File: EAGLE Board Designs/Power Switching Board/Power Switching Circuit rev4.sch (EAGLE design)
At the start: 20 parts, among them Q1 TRANSISTOR_N_MOS_2-7K1S_TK100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, Q2 TRANSISTOR_N_MOS_2-7K1S_TK100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, U1 LOGICGATE_AND_SN74AHCT1G08DBVR, U2 LOGICGATE_INVERTER_SN74AHC1GU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, U3 OPAMP_1_CHANNEL_OPA991, U4 OPAMP_1_CHANNEL_OPA991

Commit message: Created new rev4, removed DCDC, SHDN LED
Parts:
- removed D1: TVS_15V, HyTechDevices:TVS_15V
- removed U$1, U$2: LTC4359IMS8#TRPBF, HyTechDevicesTemp:LTC4359IMS8#TRPBF
- removed U2: LOGICGATE_INVERTER_SN74AHC1GU04DCK3, HyTechDevices:LOGICGATE_INVERTER_SN74AHC1GU04DCK3
- removed U3, U4: OPAMP_1_CHANNEL_OPA991, HyTechDevices:OPAMP_1_CHANNEL_OPA991
- added C10: CAPACITOR_0603_25V_0.1UF, HyTechDevices:CAPACITOR_0603_25V_0.1UF
- added C11: CAPACITOR_0603_10V_1UF, HyTechDevices:CAPACITOR_0603_10V_1UF
- added C12: CAPACITOR_0603_35V_1UF, HyTechDevices:CAPACITOR_0603_35V_1UF
- added C13, C8: CAPACITOR_0603_10V_68NF, HyTechDevices:CAPACITOR_0603_10V_68NF
- added C5, C6: CAPACITOR_0603_25V_47NF, HyTechDevices:CAPACITOR_0603_25V_47NF
- added C7: CAPACITOR_0603_25V_10UF, HyTechDevices:CAPACITOR_0603_25V_10UF
- added C9: CAPACITOR_0603_10V_680PF, HyTechDevices:CAPACITOR_0603_10V_680PF
- added D11, D12: LED_0603_GREEN, HyTechDevices:LED_0603_GREEN
- added D13, D14: LED_0603_YELLOW, HyTechDevices:LED_0603_YELLOW
- added D15, D16: LED_0603_RED, HyTechDevices:LED_0603_RED
- added D17, D7, D8, D9: LED_0603_BLUE, HyTechDevices:LED_0603_BLUE
- added D3: SCHOTTKY_SOD323_30V, HyTechDevices:SCHOTTKY_SOD323_30V
- added D4, D5, D6: TVS_15V, HyTechDevices:TVS_15V
- added J1, J3: CONNECTOR-4_SOURIAU_, HyTechDevices:CONNECTOR-4_SOURIAU_
- added J2: CONNECTOR-3_8STA20435PN, HyTechDevices:CONNECTOR-3_8STA20435PN
- added K1: RELAY_SOLIDSTATE_NO_CMX60D20, HyTechDevicesTemp:RELAY_SOLIDSTATE_NO_CMX60D20
- added Q3, Q4: TRANSISTOR_N_MOS_2-7K1S_TK100S04N1LLQ, HyTechDevices:TRANSISTOR_N_MOS_2-7K1S_TK100S04N1LLQ
- added R10, R25: RESISTOR_0603_5.49K, HyTechDevices:RESISTOR_0603_5.49K
- added R11, R26: RESISTOR_0603_1.13M, HyTechDevices:RESISTOR_0603_1.13M
- added R12, R13, R14, R16, R17, R18, R19, R20, R21: RESISTOR_0603_1K, HyTechDevices:RESISTOR_0603_1K
- added R22: RESISTOR_0603_10K, HyTechDevices:RESISTOR_0603_10K
- added R23, R7: RESISTOR_0603_41.2K, HyTechDevices:RESISTOR_0603_41.2K
- added R24, R9: RESISTOR_0603_13K, HyTechDevices:RESISTOR_0603_13K
- added R8: RESISTOR_0805_0.62, HyTechDevices:RESISTOR_0805_0.62
- added TP1, TP10, TP11, TP12, TP2, TP3, TP4, TP5, TP6, TP7, TP8, TP9: TEST_POINT, HyTechDevices:TEST_POINT
- added XF1, XF2, XF3, XF4: FUSE_HOLDER_MINIBLADEPTH, HyTechDevices:FUSE_HOLDER_MINIBLADEPTH
- C1: value CAPACITOR_0603_25V_1UF -> EEUFP1E681; device HyTechDevices:CAPACITOR_0603_25V_1UF -> HyTechDevicesTemp:EEUFP1E681
- C2, C4: value CAPACITOR_0603_25V_1UF -> CAPACITOR_0603_25V_10UF; device HyTechDevices:CAPACITOR_0603_25V_1UF -> HyTechDevices:CAPACITOR_0603_25V_10UF
- D2: value TVS_15V -> SCHOTTKY_SOD323_30V; device HyTechDevices:TVS_15V -> HyTechDevices:SCHOTTKY_SOD323_30V
- R1, R2: value RESISTOR_0603_1K -> RESISTOR_0603_10K; device HyTechDevices:RESISTOR_0603_1K -> HyTechDevices:RESISTOR_0603_10K
- R4, R5: value RESISTOR_0603_10K -> RESISTOR_SENSE__WSL40262L000FEB; device HyTechDevices:RESISTOR_0603_10K -> HyTechDevicesTemp:RESISTOR_SENSE__WSL40262L000FEB
- R6: value RESISTOR_0603_10K -> RESISTOR_0805_0.62; device HyTechDevices:RESISTOR_0603_10K -> HyTechDevices:RESISTOR_0805_0.62
- U1: value LOGICGATE_AND_SN74AHCT1G08DBVR -> LTC4421; device HyTechDevices:LOGICGATE_AND_SN74AHCT1G08DBVR -> HyTechDevices:LTC4421
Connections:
- removed net +5V: U1P.VDD, U2P.VDD, U3A.VIN-, U3P.VDD, U4A.VIN-, U4P.VDD
- removed net N$10: U$2.!SHDN
- removed net N$14: R3.1, R4.2, U3A.VIN+
- removed net N$16: R3.2
- new net !CH1: D13.C, U1.!CH1
- new net !CH2: D14.C, U1.!CH2
- new net !FAULT1: D15.C, U1.!FAULT1
- new net !FAULT2: D16.C, U1.!FAULT2
- new net !SHDN: D2.C, D3.C, K1.CONTROL+, R3.2, TP11.1, U1.!DISABLE1, U1.!DISABLE2, U1.!SHDN
- new net !VALID1: D11.C, U1.!VALID1
- new net !VALID2: D12.C, U1.!VALID2
- new net BATTERY: J1.1, J1.2, TP1.1, XF1.2, XF2.1
- new net BATTIN: D5.C, K1.CONTACT2, Q3.D, R11.2, R13.2, R6.2, U1.V2
- new net CONVOUT: TP8.1
- new net CPO: C12.2, TP12.1, U1.CPO
- new net DCDC_VICOR: J3.1, J3.2, TP4.1, XF4.1
- new net DCDC_VICORPREMOS: D6.C, Q4.D, R12.2, R26.2, R8.2, U1.V1, XF4.2
- new net GATE1: C6.2, Q1.G, Q4.G, TP9.1, U1.GATE1
- new net GATE2: C5.2, Q2.G, Q3.G, TP2.1, U1.GATE2
- new net GLVMS: D2.A, J2.2, R2.2
- new net INTVDD: C11.1, R14.2, TP3.1, U1.CASIN, U1.INTVDD
- new net N$17: D13.A, R18.1
- new net N$18: R5.3, U1.SENSE2
- new net N$19: D12.A, R17.1
- new net N$20: R5.4, U1.OUT2
- new net N$21: D11.A, R16.1
- new net N$22: C7.1, R8.1
- new net N$23: R4.3, U1.SENSE1
- new net N$24: R24.2, R25.1, U1.UVR1
- new net N$25: R23.2, R24.1, U1.OV1
- new net N$26: R10.2, R11.1, U1.UVF2
- new net N$27: R10.1, R9.2, U1.UVR2
- new net N$28: R7.2, R9.1, U1.OV2
- new net N$30: Q2.D, R5.1
- new net N$31: R4.4, U1.OUT1
- new net N$33: Q1.D, R4.1
- new net OUT: J1.3, J1.4, TP7.1, XF2.2, XF3.2
- new net OUTPREFUSE: C1.PLUS, C10.2, C12.1, C2.1, C3.1, D4.C, R22.2, R4.2, R5.2, U1.CPOREF, U1.EXTVDD, XF3.1
- new net SOURCE1: C6.1, Q1.S, Q4.S, TP10.1, U1.SOURCE1
- new net SOURCE2: C5.1, Q2.S, Q3.S, TP5.1, U1.SOURCE2
- new net START: D3.A, J2.3, R1.2
- new net UVF1: R25.2, R26.1, U1.UVF1
- net GND: now also C1.MINUS, C10.1, C11.2, C13.2, C2.2, C3.2, C4.2, C7.2, C8.2, C9.2, D17.C, D4.A, D5.A, D6.A, D7.C, D8.C, D9.C, J2.1, K1.CONTROL-, R23.1, R3.1, R7.1, TP6.1, U1.GND, U1.RETRY; no longer R4.1, R6.1, U1P.GND, U2P.GND, U3P.GND, U4P.GND
- net N$1: now also C9.1, U1.QUAL; no longer Q1.G, U$1.GATE
- net N$11: now also D16.A, R21.1; no longer U2A.IN, U4A.VOUT
- net N$12: now also K1.CONTACT1, XF1.1; no longer U1A.IN1, U3A.VOUT
- net N$13: now also D15.A, R20.1; no longer R5.1, R6.2, U4A.VIN+
- net N$15: now also D14.A, R19.1; no longer R5.2
- net N$2: now also C13.1, U1.TMR1; no longer Q2.G, U$2.GATE
- net N$3: now also C8.1, U1.TMR2; no longer C1.1, C2.1, C3.1, C4.1, Q1.D, Q2.D, U$1.OUT, U$2.OUT
- net N$4: now also C4.1, R6.1; no longer U1A.IN2, U2A.!IN
- net N$5: now also D17.A, R22.1; no longer D1.C, Q1.S, U$1.IN, U$1.SOURCE
- net N$6: now also D8.A, R13.1; no longer D2.C, Q2.S, U$2.IN, U$2.SOURCE
- net N$7: now also D7.A, R12.1; no longer C3.2, C4.2, D1.A, R1.2, U$1.VSS
- net N$8: now also R16.2, R17.2, R18.2, R19.2, R20.2, R21.2; no longer C1.2, C2.2, D2.A, R2.2, U$2.VSS
- net N$9: now also D9.A, R14.1; no longer U$1.!SHDN, U1A.OUT
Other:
- note added: "10A Fuse"
- note added: "DCDC_VICOR: OV Rising: 14.44V OV Falling: 12.34V UV Rising: 10.98V UV Falling: 9.97V CONVOUT: OV Rising: 14.44V OV Falling: 12.34V UV Rising: 10.98V UV Falling: 9.97V"
- note added: "ILim = 12.5A"
- note added: "VALID1: DCDC_VICOR is within OV/UV for time tValid VALID2: CONVOUT is within OV/UV for time tValid CH1: DCDC_VICOR is the output CH2: CONVOUT is the output FAULT1: Current limit fault on DCDC_VICOR FAULT2: Current limit fault on CONVOUT"
- note added: "tTMR,FLT = 5.644ms"
- note added: "tValid = 10.88ms"

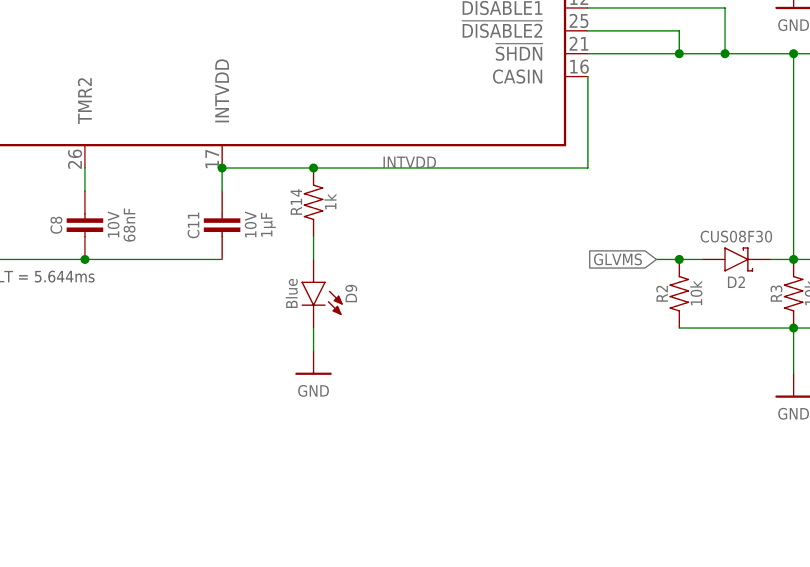
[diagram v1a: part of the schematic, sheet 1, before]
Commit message: Removed INTVDD LED
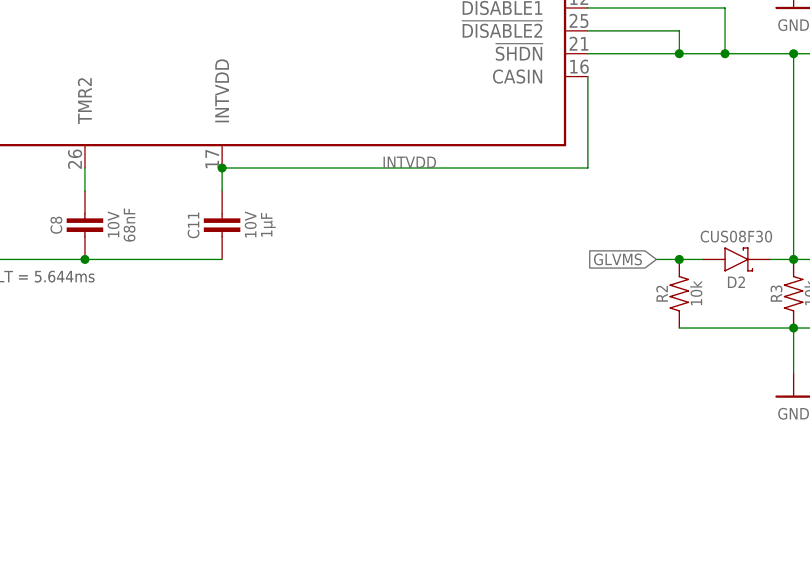
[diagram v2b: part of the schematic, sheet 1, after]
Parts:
- removed D9: LED_0603_BLUE, HyTechDevices:LED_0603_BLUE
- removed R14: RESISTOR_0603_1K, HyTechDevices:RESISTOR_0603_1K
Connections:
- removed net N$9: D9.A, R14.1
- net GND: no longer D9.C
- net INTVDD: no longer R14.2
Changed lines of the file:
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@@
 <part name="R22" library="HyTechDevices" deviceset="RESISTOR_?_*" device="0603" technology="10K"/>
 <part name="R3" library="HyTechDevices" deviceset="RESISTOR_?_*" device="0603" technology="10K"/>
-<part name="R14" library="HyTechDevices" deviceset="RESISTOR_?_*" device="0603" technology="1K"/>
 <part name="R21" library="HyTechDevices" deviceset="RESISTOR_?_*" device="0603" technology="1K"/>
 <part name="R20" library="HyTechDevices" deviceset="RESISTOR_?_*" device="0603" technology="1K"/>
@@
 <part name="D12" library="HyTechDevices" deviceset="LED_?_*" device="0603" technology="GREEN"/>
 <part name="D11" library="HyTechDevices" deviceset="LED_?_*" device="0603" technology="GREEN"/>
-<part name="D9" library="HyTechDevices" deviceset="LED_?_*" device="0603" technology="BLUE" value="LED_0603_BLUE"/>
 <part name="P2" library="HyTechSupplies" deviceset="GND" device=""/>
 <part name="P1" library="HyTechSupplies" deviceset="GND" device=""/>
@@
 <part name="P9" library="HyTechSupplies" deviceset="GND" device=""/>
 <part name="P10" library="HyTechSupplies" deviceset="GND" device=""/>
-<part name="P11" library="HyTechSupplies" deviceset="GND" device=""/>
 <part name="P12" library="HyTechSupplies" deviceset="GND" device=""/>
 <part name="P13" library="HyTechSupplies" deviceset="GND" device=""/>
@@
 <attribute name="RESISTANCE" x="80.01" y="-74.93" size="1.27" layer="96" rot="R90" align="top-center"/>
 </instance>
-<instance part="R14" gate="G$1" x="25.4" y="-63.5" smashed="yes" rot="R90">
-<attribute name="NAME" x="24.13" y="-64.77" size="1.27" layer="95" rot="R90" align="bottom-center"/>
-<attribute name="RESISTANCE" x="26.67" y="-64.77" size="1.27" layer="96" rot="R90" align="top-center"/>
-</instance>
 <instance part="R21" gate="G$1" x="99.06" y="-33.02" smashed="yes">
 <attribute name="NAME" x="97.79" y="-31.75" size="1.27" layer="95" align="bottom-center"/>
@@
 <attribute name="NAME" x="87.63" y="-23.876" size="1.27" layer="96" rot="R180" align="bottom-center"/>
 </instance>
-<instance part="D9" gate="LED" x="25.4" y="-76.2" smashed="yes" rot="R270">
-<attribute name="COLOR" x="23.622" y="-74.93" size="1.27" layer="95" rot="R270" align="top-center"/>
-<attribute name="NAME" x="28.956" y="-74.93" size="1.27" layer="96" rot="R270" align="bottom-center"/>
-</instance>
 <instance part="P2" gate="1" x="-111.76" y="-83.82" smashed="yes">
 <attribute name="VALUE" x="-111.76" y="-85.09" size="1.27" layer="96" align="top-center"/>
@@
 <instance part="P10" gate="1" x="78.74" y="-43.18" smashed="yes">
 <attribute name="VALUE" x="78.74" y="-44.45" size="1.27" layer="96" align="top-center"/>
-</instance>
-<instance part="P11" gate="1" x="25.4" y="-83.82" smashed="yes">
-<attribute name="VALUE" x="25.4" y="-85.09" size="1.27" layer="96" align="top-center"/>
 </instance>
 <instance part="P12" gate="1" x="78.74" y="-86.36" smashed="yes">
@@
 <wire x1="55.88" y1="-40.64" x2="78.74" y2="-40.64" width="0.1524" layer="91"/>
 <pinref part="P10" gate="1" pin="GND"/>
-</segment>
-<segment>
-<wire x1="25.4" y1="-78.74" x2="25.4" y2="-81.28" width="0.1524" layer="91"/>
-<pinref part="D9" gate="LED" pin="C"/>
-<pinref part="P11" gate="1" pin="GND"/>
 </segment>
 <segment>
@@
 </segment>
 </net>
-<net name="N$9" class="0">
-<segment>
-<wire x1="25.4" y1="-71.12" x2="25.4" y2="-68.58" width="0.1524" layer="91"/>
-<pinref part="R14" gate="G$1" pin="1"/>
-<pinref part="D9" gate="LED" pin="A"/>
-</segment>
-</net>
 <net name="N$18" class="0">
 <segment>
@@
 <segment>
 <pinref part="U1" gate="G$1" pin="INTVDD"/>
-<wire x1="25.4" y1="-60.96" x2="15.24" y2="-60.96" width="0.1524" layer="91"/>
-<wire x1="25.4" y1="-60.96" x2="55.88" y2="-60.96" width="0.1524" layer="91"/>
+<wire x1="15.24" y1="-60.96" x2="55.88" y2="-60.96" width="0.1524" layer="91"/>
 <pinref part="C11" gate="G$1" pin="1"/>
 <junction x="15.24" y="-60.96"/>
-<pinref part="R14" gate="G$1" pin="2"/>
-<junction x="25.4" y="-60.96"/>
 <wire x1="15.24" y1="-63.5" x2="15.24" y2="-60.96" width="0.1524" layer="91"/>
 <pinref part="U1" gate="G$1" pin="CASIN"/>

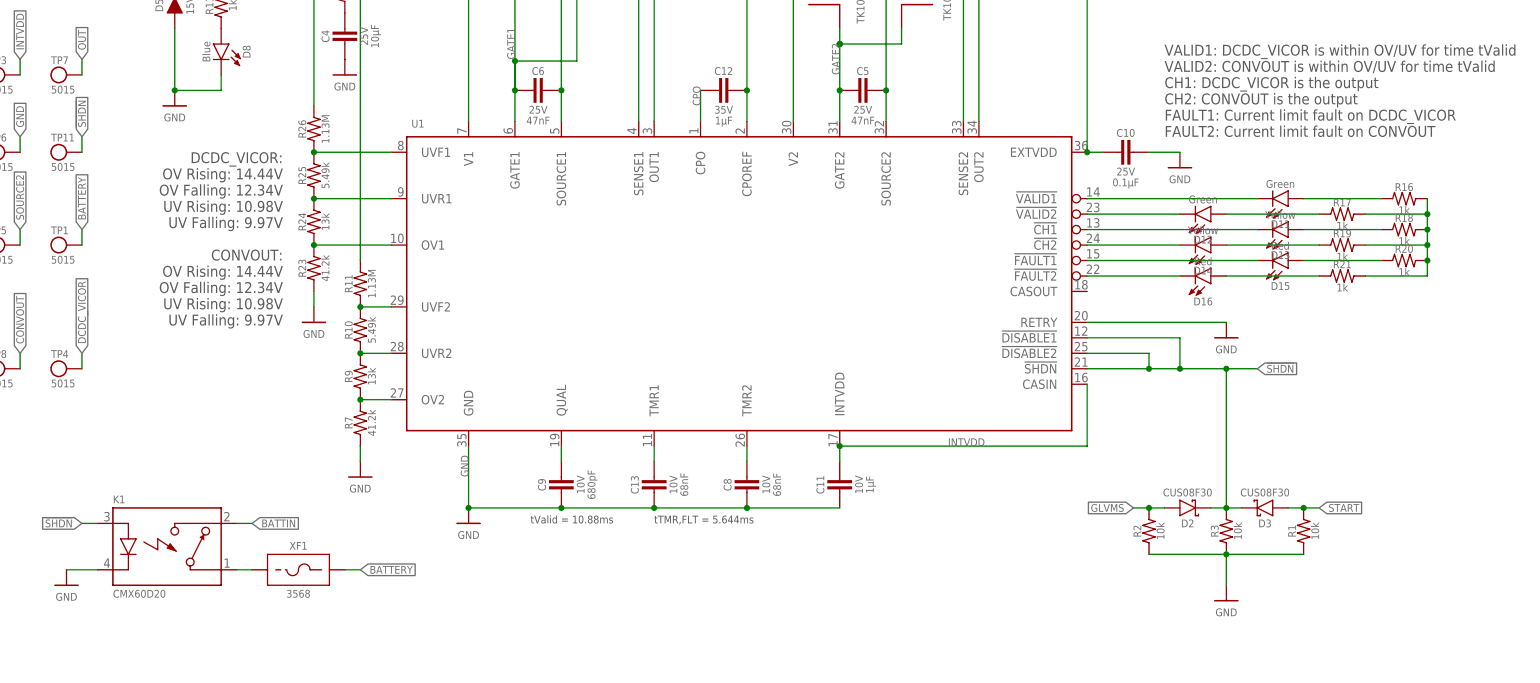
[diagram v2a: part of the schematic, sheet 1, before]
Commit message: Replaced sense resistors
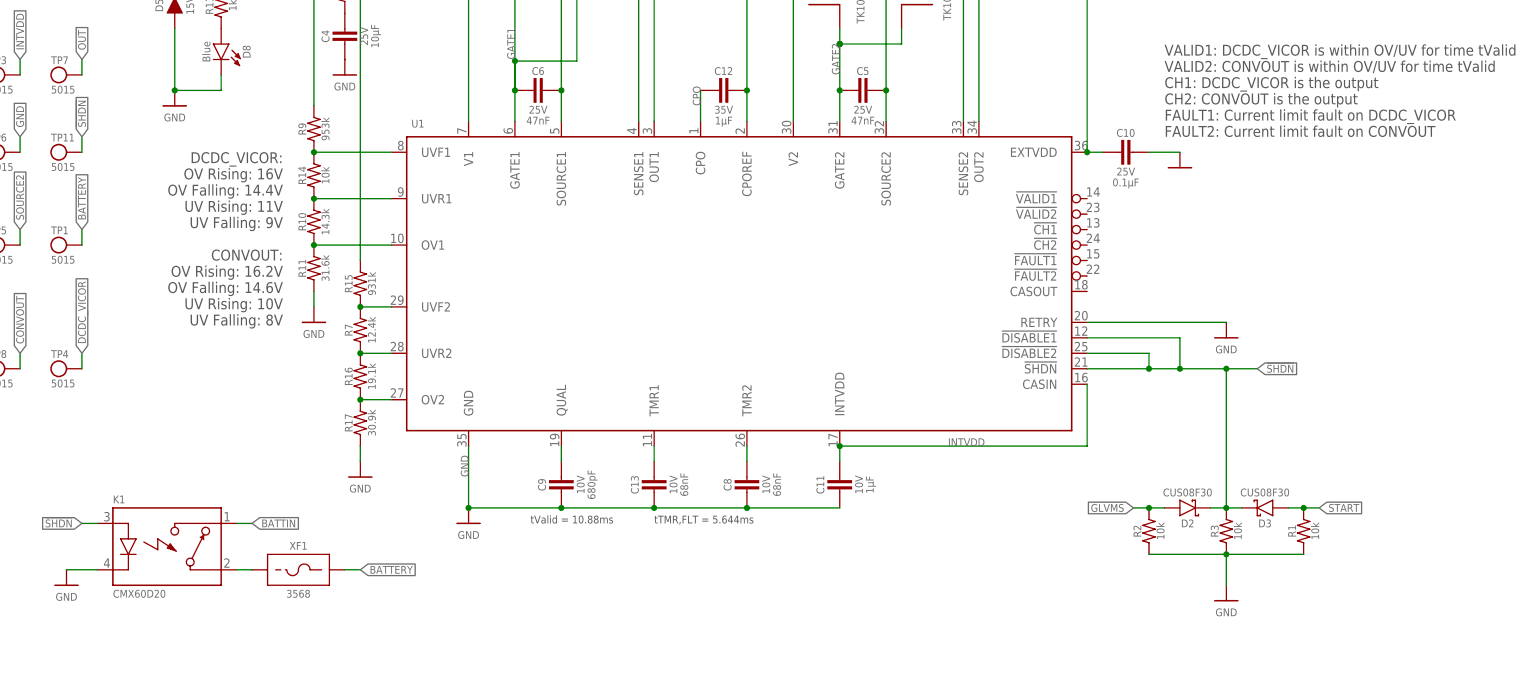
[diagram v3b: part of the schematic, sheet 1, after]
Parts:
- removed D11, D12: LED_0603_GREEN, HyTechDevices:LED_0603_GREEN
- removed D13, D14: LED_0603_YELLOW, HyTechDevices:LED_0603_YELLOW
- removed D15, D16: LED_0603_RED, HyTechDevices:LED_0603_RED
- removed R18, R19, R20, R21: RESISTOR_0603_1K, HyTechDevices:RESISTOR_0603_1K
- removed R23: RESISTOR_0603_41.2K, HyTechDevices:RESISTOR_0603_41.2K
- removed R24: RESISTOR_0603_13K, HyTechDevices:RESISTOR_0603_13K
- removed R25: RESISTOR_0603_5.49K, HyTechDevices:RESISTOR_0603_5.49K
- removed R26: RESISTOR_0603_1.13M, HyTechDevices:RESISTOR_0603_1.13M
- added R14: RESISTOR_0603_10K, HyTechDevices:RESISTOR_0603_10K
- added R15: RESISTOR_0805_931K, HyTechDevices:RESISTOR_0805_931K
- R10: value RESISTOR_0603_5.49K -> RESISTOR_0805_14.3K; device HyTechDevices:RESISTOR_0603_5.49K -> HyTechDevices:RESISTOR_0805_14.3K
- R11: value RESISTOR_0603_1.13M -> RESISTOR_0805_31.6K; device HyTechDevices:RESISTOR_0603_1.13M -> HyTechDevices:RESISTOR_0805_31.6K
- R16: value RESISTOR_0603_1K -> RESISTOR_0805_19.1K; device HyTechDevices:RESISTOR_0603_1K -> HyTechDevices:RESISTOR_0805_19.1K
- R17: value RESISTOR_0603_1K -> RESISTOR_0603_30.9K; device HyTechDevices:RESISTOR_0603_1K -> HyTechDevices:RESISTOR_0603_30.9K
- R7: value RESISTOR_0603_41.2K -> RESISTOR_0603_12.4K; device HyTechDevices:RESISTOR_0603_41.2K -> HyTechDevices:RESISTOR_0603_12.4K
- R9: value RESISTOR_0603_13K -> RESISTOR_0805_953K; device HyTechDevices:RESISTOR_0603_13K -> HyTechDevices:RESISTOR_0805_953K
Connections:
- removed net !CH1: D13.C, U1.!CH1
- removed net !CH2: D14.C, U1.!CH2
- removed net !FAULT1: D15.C, U1.!FAULT1
- removed net !FAULT2: D16.C, U1.!FAULT2
- removed net !VALID1: D11.C, U1.!VALID1
- removed net !VALID2: D12.C, U1.!VALID2
- removed net N$11: D16.A, R21.1
- removed net N$13: D15.A, R20.1
- removed net N$15: D14.A, R19.1
- removed net N$17: D13.A, R18.1
- removed net N$19: D12.A, R17.1
- removed net N$21: D11.A, R16.1
- removed net N$8: R16.2, R17.2, R18.2, R19.2, R20.2, R21.2
- net BATTIN: now also R15.2; no longer R11.2
- net DCDC_VICORPREMOS: now also R9.2; no longer R26.2
- net GND: now also R11.1, R17.1; no longer R23.1, R7.1
- net N$24: now also R10.2, R14.1; no longer R24.2, R25.1
- net N$25: now also R10.1, R11.2; no longer R23.2, R24.1
- net N$26: now also R15.1, R7.2; no longer R10.2, R11.1
- net N$27: now also R16.2, R7.1; no longer R10.1, R9.2
- net N$28: now also R16.1, R17.2; no longer R7.2, R9.1
- net UVF1: now also R14.2, R9.1; no longer R25.2, R26.1
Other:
- note added: "DCDC_VICOR: OV Rising: 16V OV Falling: 14.4V UV Rising: 11V UV Falling: 9V CONVOUT: OV Rising: 16.2V OV Falling: 14.6V UV Rising: 10V UV Falling: 8V"
- note removed: "DCDC_VICOR: OV Rising: 14.44V OV Falling: 12.34V UV Rising: 10.98V UV Falling: 9.97V CONVOUT: OV Rising: 14.44V OV Falling: 12.34V UV Rising: 10.98V UV Falling: 9.97V"
- moved on the sheet: R10, R11, R16, R17, R7, R9

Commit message: Board design part 2
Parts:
- removed TP8: TEST_POINT, HyTechDevices:TEST_POINT
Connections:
- removed net CONVOUT: TP8.1
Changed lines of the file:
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@@
 <part name="TP11" library="HyTechDevices" deviceset="TEST_POINT" device=""/>
 <part name="TP7" library="HyTechDevices" deviceset="TEST_POINT" device=""/>
-<part name="TP8" library="HyTechDevices" deviceset="TEST_POINT" device=""/>
 <part name="TP4" library="HyTechDevices" deviceset="TEST_POINT" device=""/>
 <part name="TP10" library="HyTechDevices" deviceset="TEST_POINT" device=""/>
@@
 <attribute name="MPN" x="-114.3" y="-1.778" size="1.27" layer="95" align="top-left"/>
 </instance>
-<instance part="TP8" gate="G$1" x="-121.92" y="-48.26" smashed="yes">
-<attribute name="NAME" x="-124.46" y="-46.482" size="1.27" layer="95"/>
-<attribute name="MPN" x="-124.46" y="-50.038" size="1.27" layer="95" align="top-left"/>
-</instance>
 <instance part="TP4" gate="G$1" x="-111.76" y="-48.26" smashed="yes">
 <attribute name="NAME" x="-114.3" y="-46.482" size="1.27" layer="95"/>
@@
 </segment>
 </net>
-<net name="CONVOUT" class="0">
-<segment>
-<pinref part="TP8" gate="G$1" pin="1"/>
-<wire x1="-119.38" y1="-48.26" x2="-119.38" y2="-45.72" width="0.1524" layer="91"/>
-<label x="-119.38" y="-45.72" size="1.27" layer="95" rot="R90" xref="yes"/>
-</segment>
-</net>
